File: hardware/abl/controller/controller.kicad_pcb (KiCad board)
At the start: 4 copper layers, 56.5 x 124 mm, 41 parts, among them IC1 TCA6408ARSVR, IC2 TCA6408ARSVR, IC3 VEML6040A3OG, IC4 TXB0104RUT, J1 SFW20S-2STE1LF, J2 Conn_02x05_Odd_Even, J3 Conn_02x05_Odd_Even, J4 PRT-14417, J5 Conn_02x05_Odd_Even, J6 Conn_01x10_Pin, J7 Conn_01x10_Pin, Q2 AO3401A, Q4 AO3401A, U1 INA219AxD

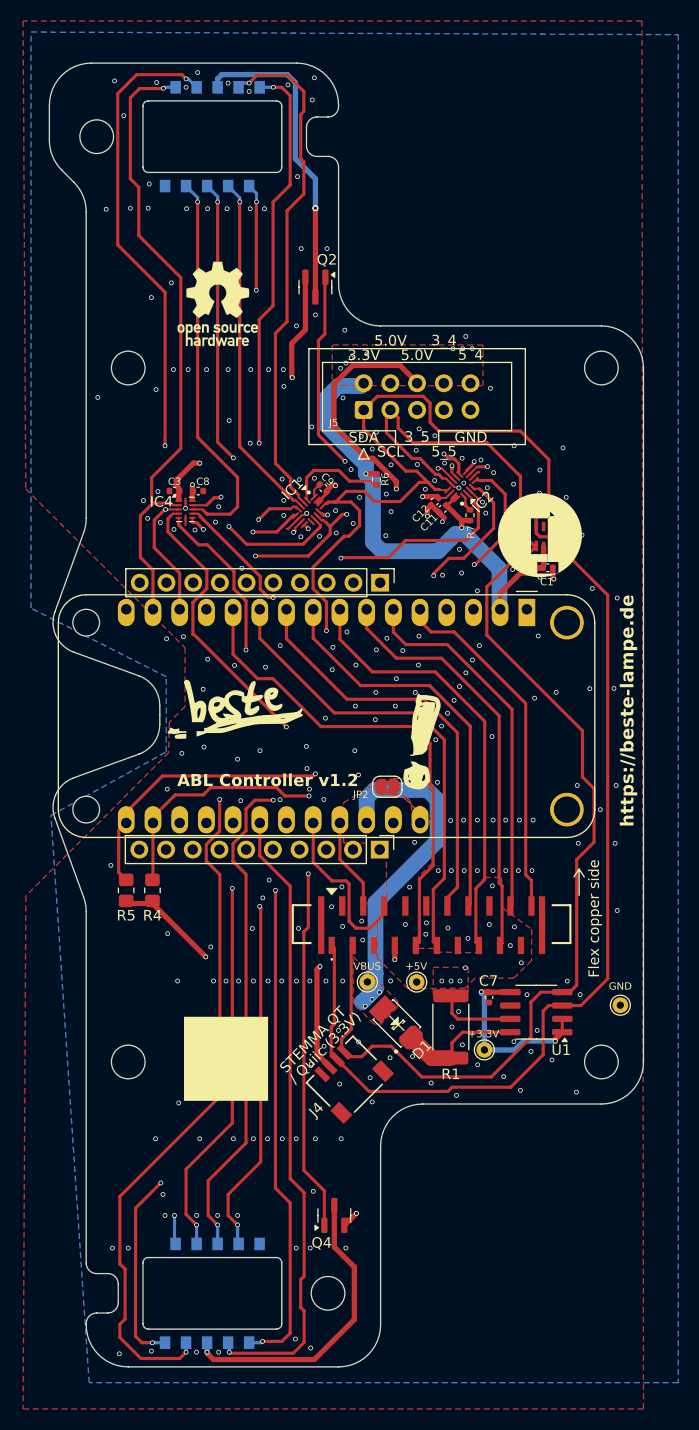
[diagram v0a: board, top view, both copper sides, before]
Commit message: Relayout controller module for final pruction run.
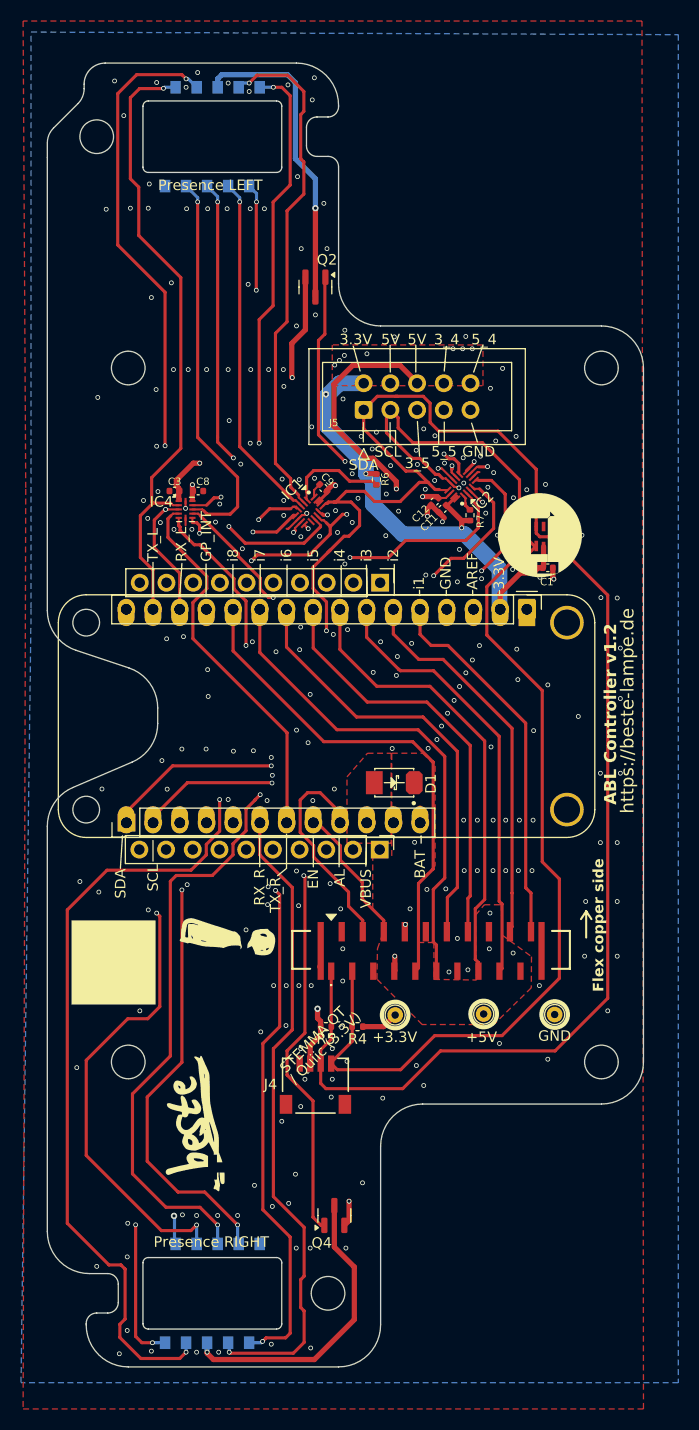
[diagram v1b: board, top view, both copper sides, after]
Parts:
- removed C7: 100nF, Capacitor_SMD:C_0402_1005Metric
- removed JP2: SolderJumper_2_Bridged, Jumper:SolderJumper-2_P1.3mm_Bridged2Bar_RoundedPad1.0x1.5mm
- removed R1: R, Resistor_SMD:R_2512_6332Metric
- removed REF**: OSHW-Logo_7.5x8mm_SilkScreen, Symbol:OSHW-Logo_7.5x8mm_SilkScreen
- removed TP4: TestPoint, TestPoint:TestPoint_THTPad_D1.5mm_Drill0.7mm
- removed U1: INA219AxD, Package_SO:SOIC-8_3.9x4.9mm_P1.27mm
- added J8: Conn_01x16, Connector_PinHeader_2.54mm:PinHeader_1x16_P2.54mm_Vertical, F.Cu at (104.9, 79.9)
- added J9: Conn_01x12, Connector_PinHeader_2.54mm:PinHeader_1x12_P2.54mm_Vertical, F.Cu at (66.8, 100.2)
- R4, R5: footprint Resistor_SMD:R_0805_2012Metric_Pad1.20x1.40mm_HandSolder -> Resistor_SMD:R_0402_1005Metric
- moved G*** 31.4 mm to (75.7, 122.1), turned to 90 degrees
- moved R4 23.4 mm to (88.8, 119.6), turned to 180 degrees
- moved R5 23.0 mm to (85.8, 119.6), turned to 180 degrees
- moved D1 22.9 mm to (92.3, 96.4), turned to 180 degrees
- moved TP2 9.11 mm to (92.4, 118.5)
- moved TP3 7.06 mm to (100.8, 118.4)
- moved TP1 6.31 mm to (107.6, 118.5)
- moved J4 3.26 mm to (84.8, 125.3), turned to 0 degrees
- moved J1 2.45 mm to (95.8, 112.4)
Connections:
- A1 pad 28: +BATT -> +5V
- D1 pad 1: Net-(D1-K) -> +5V
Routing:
- net +3.3V: track 189.2 -> 139.6 mm, vias 9 -> 7
- net VBUS: track 34.1 -> 0.00 mm, vias 3 -> 0
- net +5V: track 112.1 -> 94.2 mm, vias 21 -> 16
- net /SCL: track 194.8 -> 177.6 mm
- net /SDA: track 203.5 -> 189.9 mm
- net /ALERT: track 8.82 -> 20.8 mm
- net Net-(D1-K): track 12.0 -> 0.00 mm
- net /FX_3_3: track 79.0 -> 90.0 mm
- net /FX_3_2: track 97.9 -> 106.3 mm
- net /TX_R_5: track 78.2 -> 86.0 mm
- net /EN_LED: track 17.0 -> 13.9 mm
- net /i7: track 44.4 -> 46.8 mm
- net /i1: track 33.9 -> 36.0 mm
- net /i5: track 38.3 -> 40.3 mm
- net /i4: track 41.6 -> 43.6 mm
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- removed copper zone on F.Cu, net +BATT
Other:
- board size 56.5 x 124 mm -> 56.7 x 124 mm
- board text added: "5V"
- board text added: "AL"
- board text added: "AREF"
- board text added: "BAT"
- board text added: "EN"
- board text added: "GP_INT"
- board text added: "Presence LEFT"
- board text added: "Presence RIGHT"
- board text added: "RX_L"
- board text added: "RX_R"
- board text added: "TX_L"
- board text added: "TX_R"
- board text added: "i1"
- board text added: "i2"
- board text added: "i3"
- board text added: "i4"
- board text added: "i5"
- board text added: "i6"
- board text added: "i7"
- board text added: "i8"
- board text removed: "5.0V"

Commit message: Even more small adjustments before ordering v1.2 of controller module.
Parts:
- moved TP3 1.00 mm to (99.8, 118.4)
- moved TP1 0.75 mm to (106.8, 118.4)
- moved TP2 0.43 mm to (92.8, 118.4)
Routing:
- net /FX_5_2: track 105.6 -> 99.8 mm
- net /FX_5_3: track 94.7 -> 88.9 mm
- net /SCL: track 177.6 -> 182.8 mm
- net /FX_3_3: track 90.0 -> 88.4 mm
- net /SDA: track 189.9 -> 191.2 mm
- net /FX_3_2: track 106.3 -> 105.2 mm
- net /FX_5_6: track 31.2 -> 32.0 mm
- net /ALERT: track 20.8 -> 21.5 mm
- net +3.3V: track 139.6 -> 140.1 mm, vias 7 -> 6
- net GND: vias 250 -> 251
